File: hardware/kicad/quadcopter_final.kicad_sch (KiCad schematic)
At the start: 9 parts, among them M1 Motor_DC, M2 Motor_DC, M3 Motor_DC, M4 Motor_DC, U1 DRV8833PW, U2 DRV8833PW, U3 ICM-20948, U4 BMP280

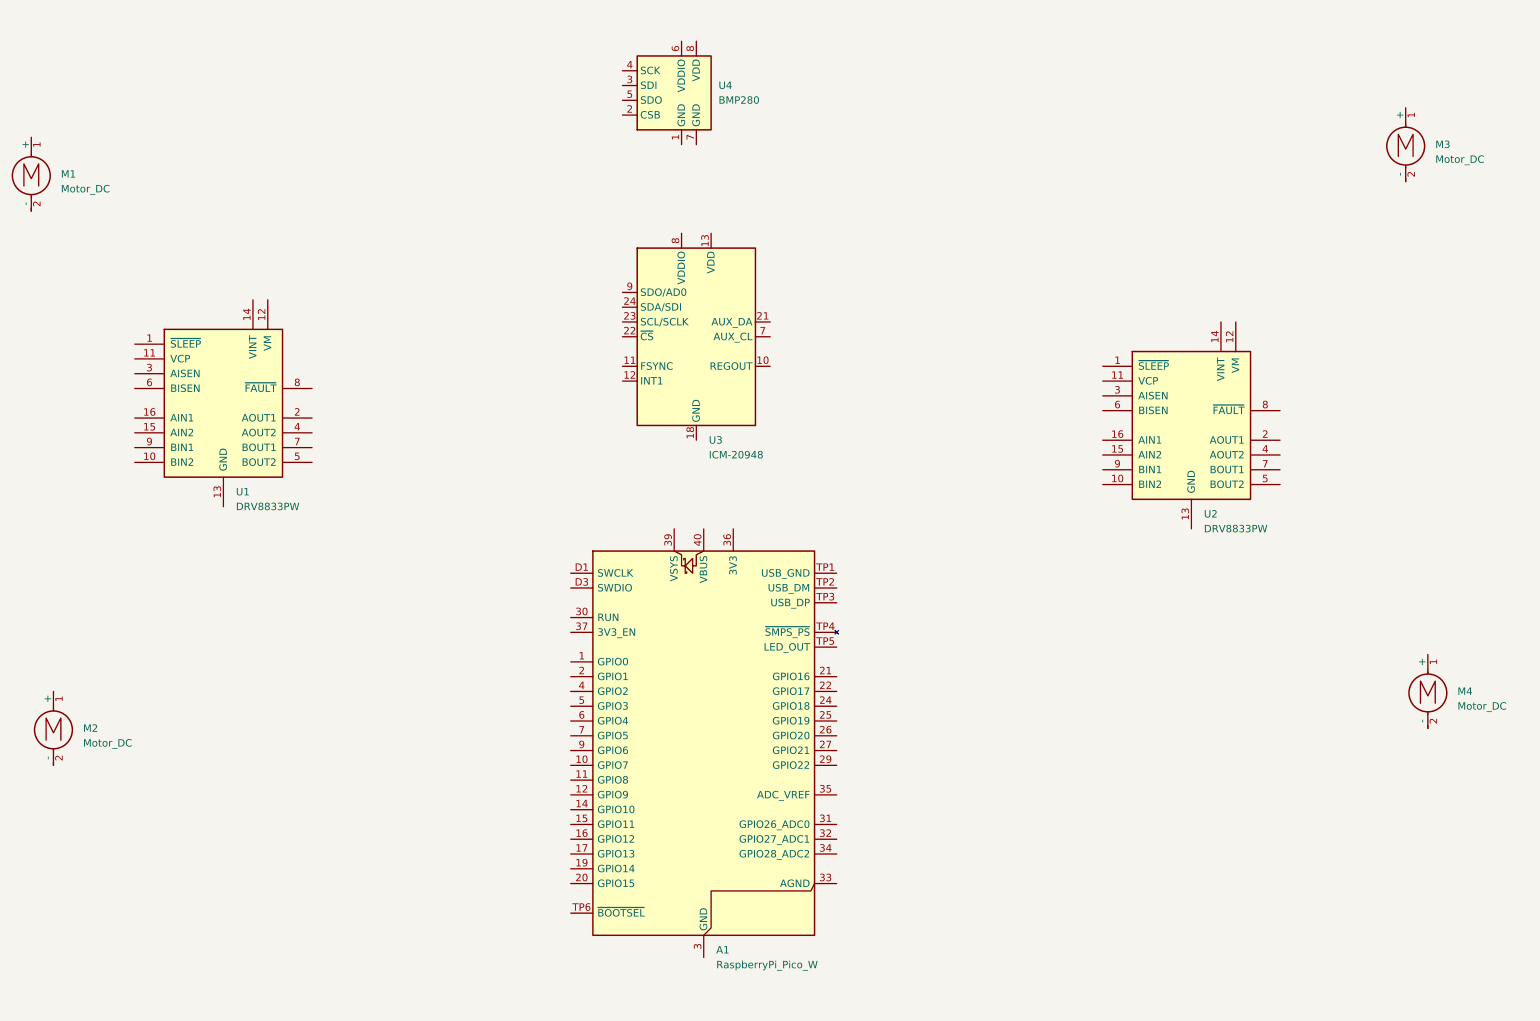
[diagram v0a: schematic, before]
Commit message: Apply Android build fixes and compose UI
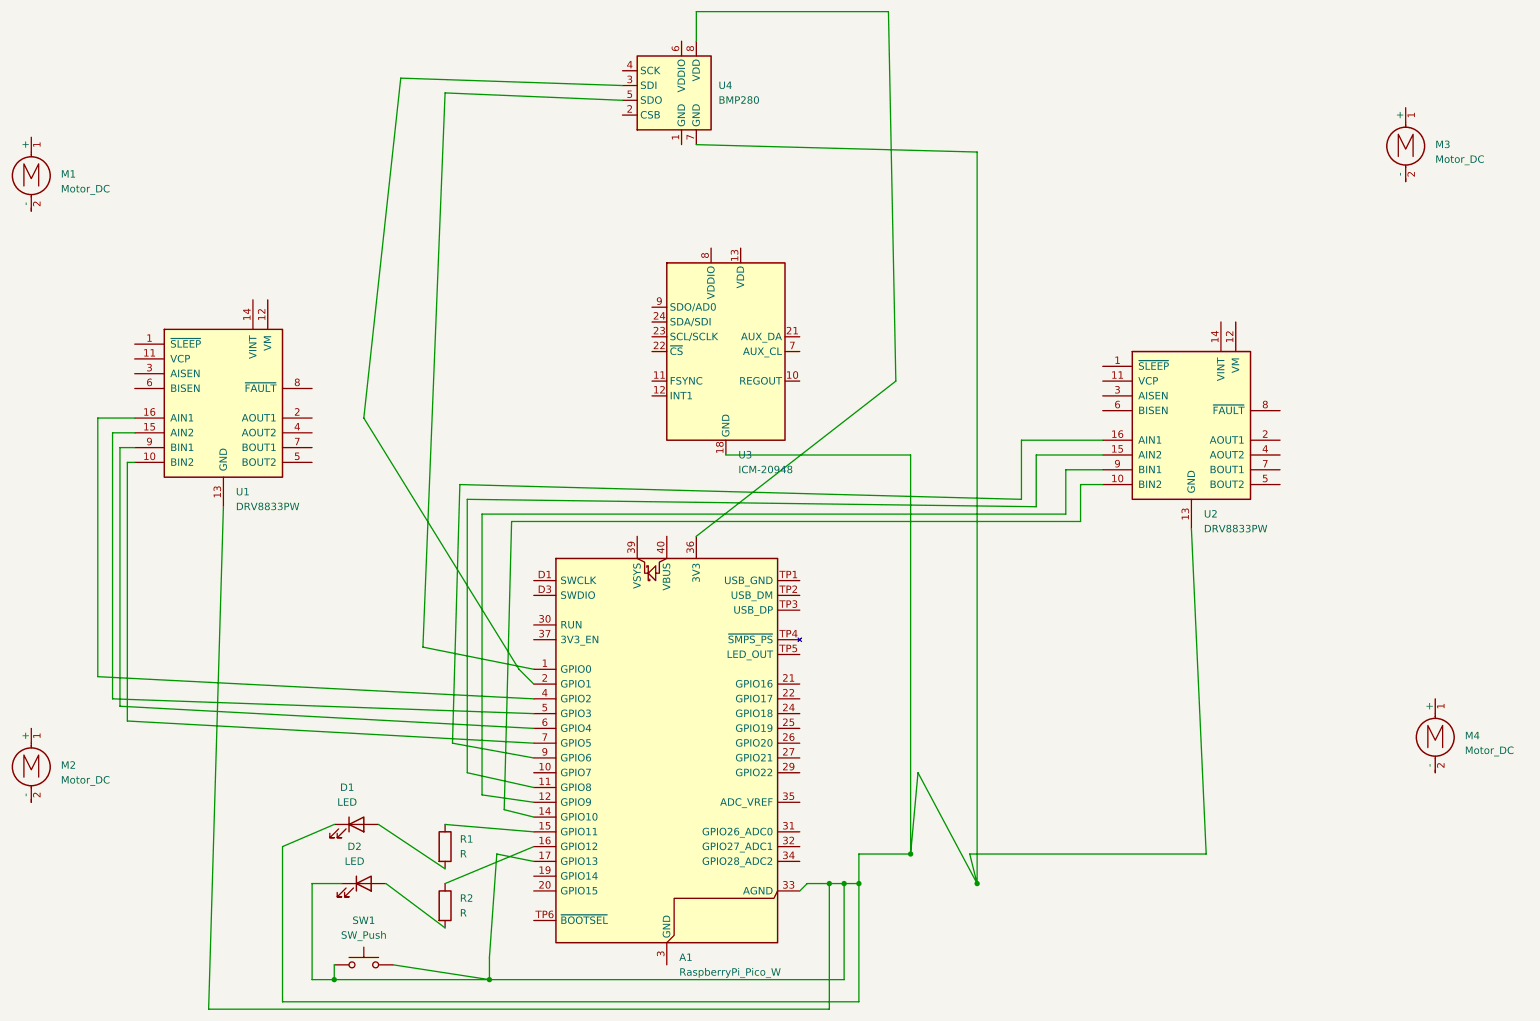
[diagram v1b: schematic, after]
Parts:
- added D1, D2: LED, symbol Device:LED
- added R1, R2: R, symbol Device:R
- added SW1: SW_Push, symbol Switch:SW_Push
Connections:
- net at U3.18 (GND), U3.20 (GND): now also A1.17 (GPIO13), A1.33 (AGND), U1.13 (GND), U2.13 (GND), U4.7 (GND), D1.1 (K), D2.1 (K), SW1.1, SW1.2
- net at A1.1 (GPIO0): now also U4.5 (SDO)
- net at A1.11 (GPIO8): now also U2.15 (AIN2)
- net at A1.12 (GPIO9): now also U2.9 (BIN1)
- net at A1.14 (GPIO10): now also U2.10 (BIN2)
- net at A1.15 (GPIO11): now also R1.1
- net at A1.16 (GPIO12): now also R2.1
- net at A1.2 (GPIO1): now also U4.3 (SDI)
- net at A1.36 (3V3): now also U4.8 (VDD)
- net at A1.4 (GPIO2): now also U1.16 (AIN1)
- net at A1.5 (GPIO3): now also U1.15 (AIN2)
- net at A1.6 (GPIO4): now also U1.9 (BIN1)
- net at A1.7 (GPIO5): now also U1.10 (BIN2)
- net at A1.9 (GPIO6): now also U2.16 (AIN1)
- new net: D2.2 (A), R2.2
- new net: D1.2 (A), R1.2
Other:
- moved on the sheet: A1, M2, M4, U3
